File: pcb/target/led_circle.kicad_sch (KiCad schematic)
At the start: 20 parts

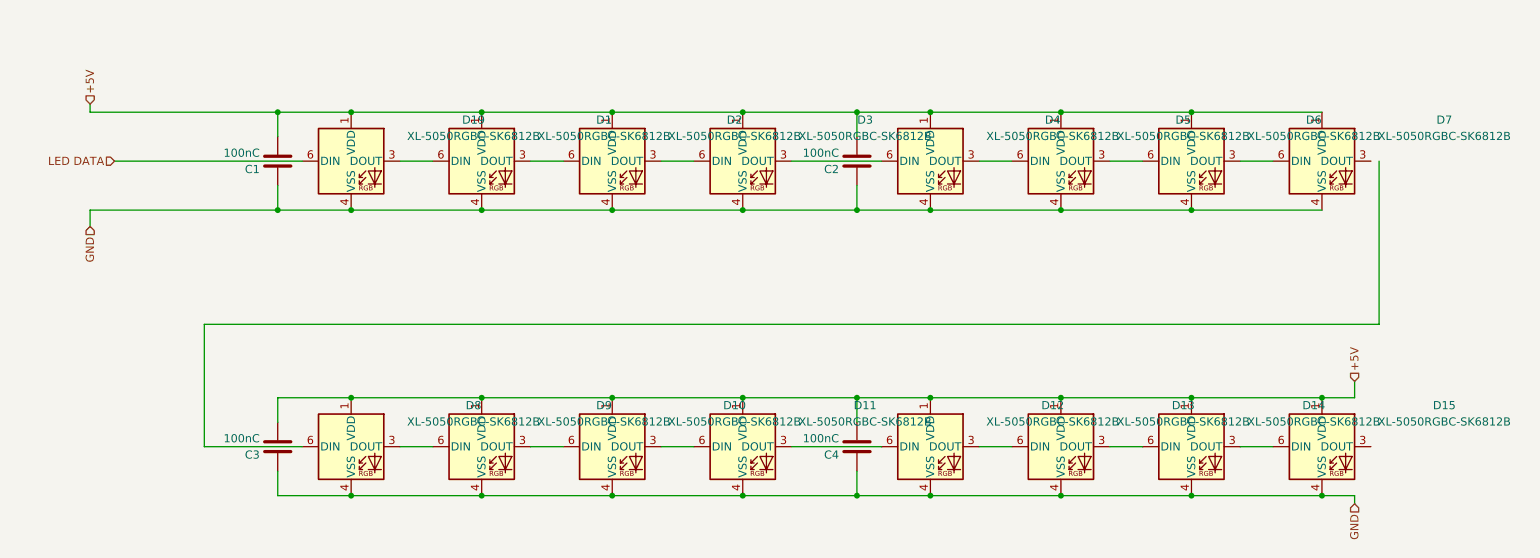
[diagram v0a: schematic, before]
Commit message: added updi connector
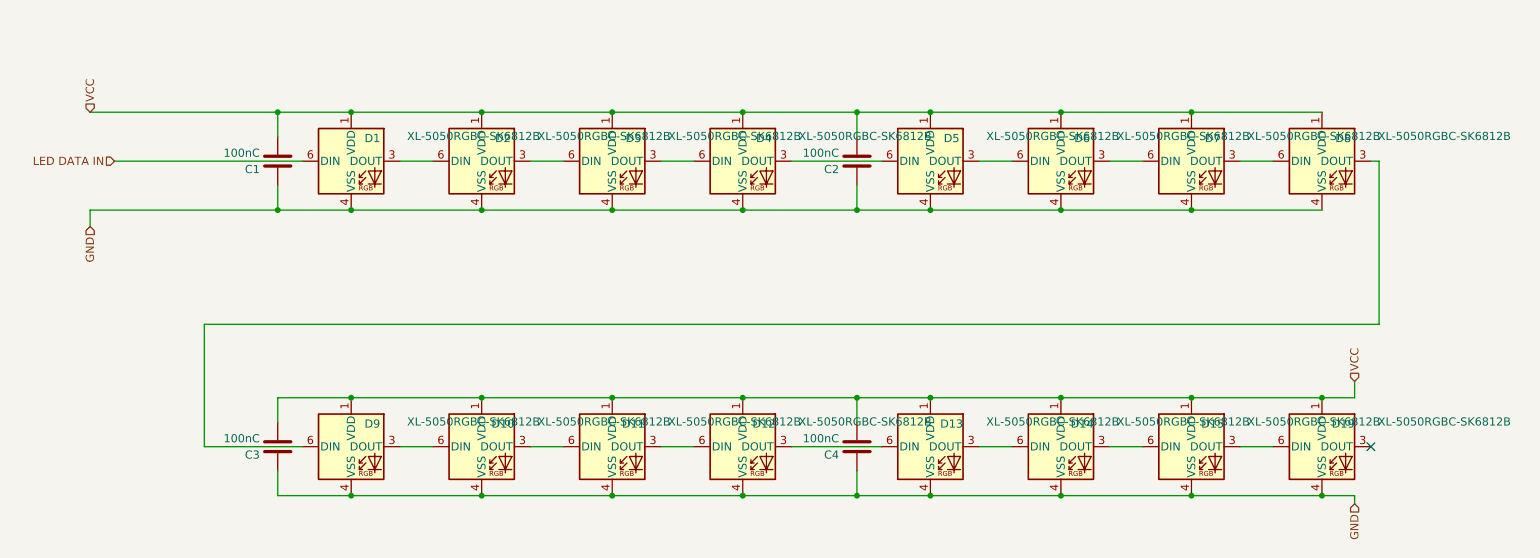
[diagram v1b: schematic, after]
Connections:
- net LED DATA is gone; now on an unnamed net: D19.6 (DIN)
- net at D7.3 (DOUT): now also D8.6 (DIN)
- net at D19.3 (DOUT): no longer D1.6 (DIN)
- net +5V renamed VCC
- new net LED DATA IN: D1.6 (DIN)
- no-connect marks 0 -> 1

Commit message: fixed some footprint issues
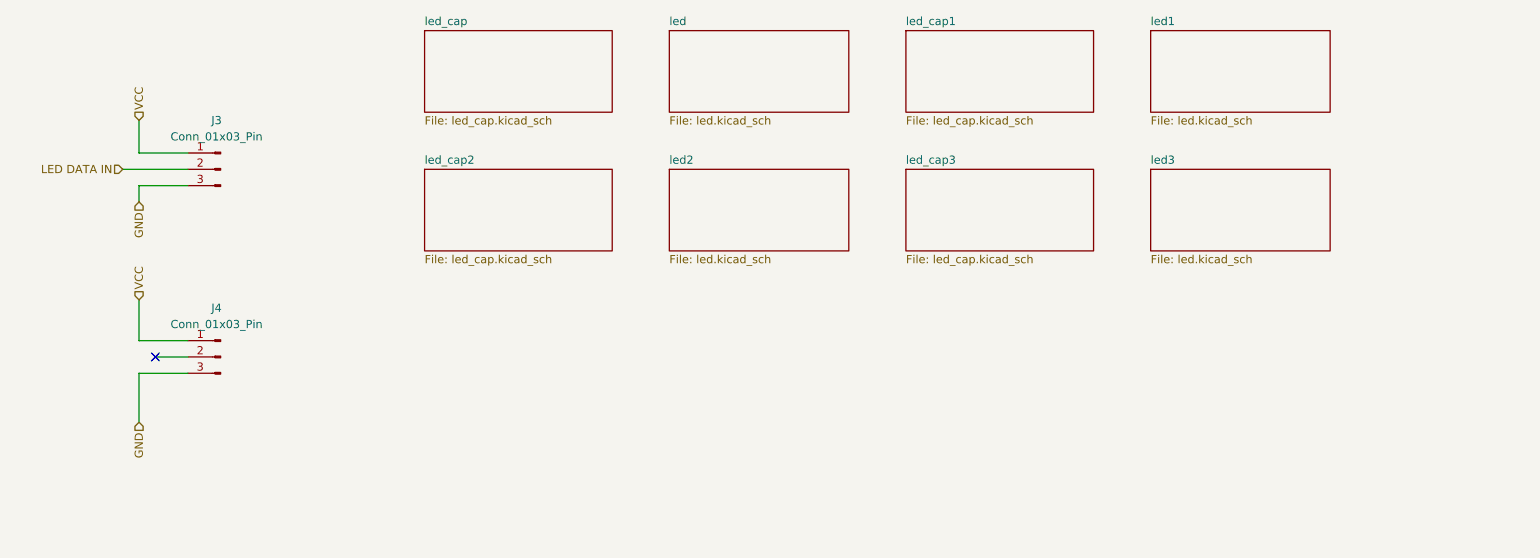
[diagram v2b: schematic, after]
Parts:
- removed C1, C2, C3, C4: 100nC, Capacitor_SMD:C_1206_3216Metric, symbol Device:C
- removed D1, D10, D11, D12, D13, D14, D15, D19, D2, D3, D4, D5, D6, D7, D8, D9: XL-5050RGBC-SK6812B, custom_footprints:XL-5050RGBC-SK6812B, symbol custom_symbols:XL-5050RGBC-SK6812B
- added J3, J4: Conn_01x03_Pin, Connector_Wire:SolderWire-0.75sqmm_1x03_P4.8mm_D1.25mm_OD2.3mm, symbol Connector:Conn_01x03_Pin
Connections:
- net GND: now also J3.3 (Pin_3), J4.3 (Pin_3)
- net LED DATA IN: now also J3.2 (Pin_2)
- net VCC: now also J3.1 (Pin_1), J4.1 (Pin_1)
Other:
- added sheet led (led.kicad_sch)
- added sheet led1 (led.kicad_sch)
- added sheet led2 (led.kicad_sch)
- added sheet led3 (led.kicad_sch)
- added sheet led_cap (led_cap.kicad_sch)
- added sheet led_cap1 (led_cap.kicad_sch)
- added sheet led_cap2 (led_cap.kicad_sch)
- added sheet led_cap3 (led_cap.kicad_sch)

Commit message: finishing up target pcb
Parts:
- J3, J4: footprint Connector_Wire:SolderWire-0.75sqmm_1x03_P4.8mm_D1.25mm_OD2.3mm -> custom_footprints:01x03 SMD 2x3mm pad
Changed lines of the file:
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@@
 			)
 		)
-		(property "Footprint" "Connector_Wire:SolderWire-0.75sqmm_1x03_P4.8mm_D1.25mm_OD2.3mm"
+		(property "Footprint" "custom_footprints:01x03 SMD 2x3mm pad"
 			(at 43.18 74.93 0)
 			(effects
@@
 			)
 		)
-		(property "Footprint" "Connector_Wire:SolderWire-0.75sqmm_1x03_P4.8mm_D1.25mm_OD2.3mm"
+		(property "Footprint" "custom_footprints:01x03 SMD 2x3mm pad"
 			(at 43.18 45.72 0)
 			(effects

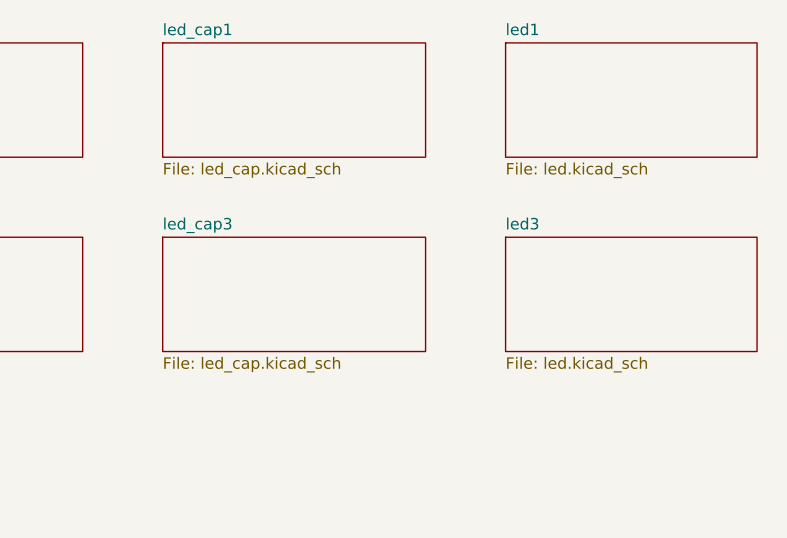
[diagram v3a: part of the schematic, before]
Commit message: added lcsc numbers to all components and added ESD protection
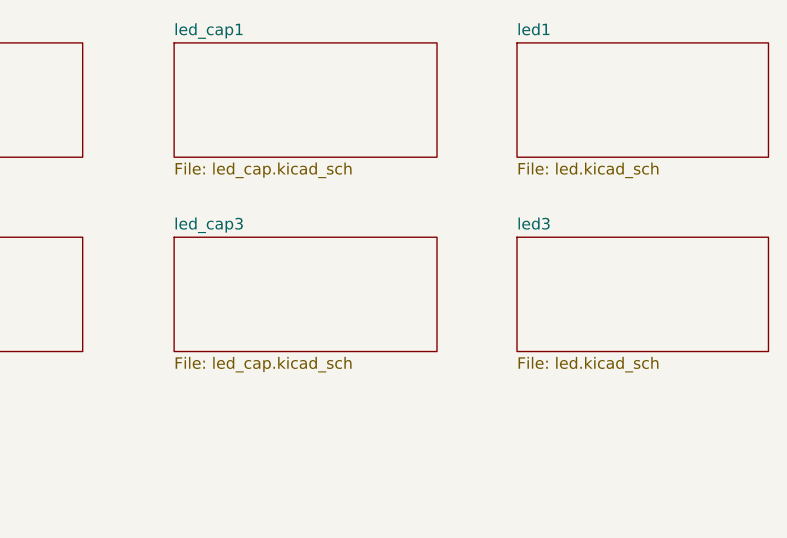
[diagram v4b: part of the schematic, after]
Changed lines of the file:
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@@
+			)
+		)
+		(property "LCSC" ""
+			(at 43.18 74.93 0)
+			(effects
+				(font
+					(size 1.27 1.27)
+				)
+				(hide yes)
 			)
 		)
@@
 			)
 		)
+		(property "LCSC" ""
+			(at 43.18 45.72 0)
+			(effects
+				(font
+					(size 1.27 1.27)
+				)
+				(hide yes)
+			)
+		)
 		(pin "3"
 		)
@@
 	)
 	(sheet
-		(at 149.86 24.13)
+		(at 151.13 24.13)
 		(size 29.21 12.7)
 		(exclude_from_sim no)
@@
 		)
 		(property "Sheetname" "led_cap1"
-			(at 149.86 23.4184 0)
+			(at 151.13 23.4184 0)
 			(effects
 				(font
@@
 		)
 		(property "Sheetfile" "led_cap.kicad_sch"
-			(at 149.86 37.4146 0)
+			(at 151.13 37.4146 0)
 			(effects
 				(font
@@
 	)
 	(sheet
-		(at 187.96 24.13)
+		(at 189.23 45.72)
 		(size 27.94 12.7)
 		(exclude_from_sim no)
@@
 			(color 0 0 0 0.0000)
 		)
-		(property "Sheetname" "led1"
-			(at 187.96 23.4184 0)
+		(property "Sheetname" "led3"
+			(at 189.23 45.0084 0)
 			(effects
 				(font
@@
 		)
 		(property "Sheetfile" "led.kicad_sch"
-			(at 187.96 37.4146 0)
-			(effects
-				(font
-					(size 1.27 1.27)
-				)
-				(justify left top)
-			)
-		)
-		(instances
-			(project "target"
-				(path "/1c02f793-f381-44cb-838a-dbb787484d0c/e61b723f-f359-4114-beb0-b4d2930b2aa9"
-					(page "6")
-				)
-			)
-		)
-	)
-	(sheet
-		(at 187.96 45.72)
-		(size 27.94 12.7)
-		(exclude_from_sim no)
-		(in_bom yes)
-		(on_board yes)
-		(dnp no)
-		(fields_autoplaced yes)
-		(stroke
-			(width 0.1524)
-			(type solid)
-		)
-		(fill
-			(color 0 0 0 0.0000)
-		)
-		(property "Sheetname" "led3"
-			(at 187.96 45.0084 0)
-			(effects
-				(font
-					(size 1.27 1.27)
-				)
-				(justify left bottom)
-			)
-		)
-		(property "Sheetfile" "led.kicad_sch"
-			(at 187.96 59.0046 0)
-			(effects
-				(font
-					(size 1.27 1.27)
-				)
-				(justify left top)
-			)
-		)
-		(instances
-			(project "target"
-				(path "/1c02f793-f381-44cb-838a-dbb787484d0c/e61b723f-f359-4114-beb0-b4d2930b2aa9"
-					(page "9")
-				)
-			)
-		)
-	)
-	(sheet
-		(at 149.86 45.72)
-		(size 29.21 12.7)
-		(exclude_from_sim no)
-		(in_bom yes)
-		(on_board yes)
-		(dnp no)
-		(fields_autoplaced yes)
-		(stroke
-			(width 0.1524)
-			(type solid)
-		)
-		(fill
-			(color 0 0 0 0.0000)
-		)
-		(property "Sheetname" "led_cap3"
-			(at 149.86 45.0084 0)
-			(effects
-				(font
-					(size 1.27 1.27)
-				)
-				(justify left bottom)
-			)
-		)
-		(property "Sheetfile" "led_cap.kicad_sch"
-			(at 149.86 59.0046 0)
-			(effects
-				(font
-					(size 1.27 1.27)
-				)
-				(justify left top)
-			)
-		)
-		(instances
-			(project "target"
-				(path "/1c02f793-f381-44cb-838a-dbb787484d0c/e61b723f-f359-4114-beb0-b4d2930b2aa9"
-					(page "11")
+			(at 189.23 59.0046 0)
+			(effects
+				(font
+					(size 1.27 1.27)
+				)
+				(justify left top)
+			)
+		)
+		(instances
+			(project "target"
+				(path "/1c02f793-f381-44cb-838a-dbb787484d0c/e61b723f-f359-4114-beb0-b4d2930b2aa9"
+					(page "10")
 				)
 			)
@@
 			(project "target"
 				(path "/1c02f793-f381-44cb-838a-dbb787484d0c/e61b723f-f359-4114-beb0-b4d2930b2aa9"
-					(page "10")
+					(page "9")
+				)
+			)
+		)
+	)
+	(sheet
+		(at 189.23 24.13)
+		(size 27.94 12.7)
+		(exclude_from_sim no)
+		(in_bom yes)
+		(on_board yes)
+		(dnp no)
+		(fields_autoplaced yes)
+		(stroke
+			(width 0.1524)
+			(type solid)
+		)
+		(fill
+			(color 0 0 0 0.0000)
+		)
+		(property "Sheetname" "led1"
+			(at 189.23 23.4184 0)
+			(effects
+				(font
+					(size 1.27 1.27)
+				)
+				(justify left bottom)
+			)
+		)
+		(property "Sheetfile" "led.kicad_sch"
+			(at 189.23 37.4146 0)
+			(effects
+				(font
+					(size 1.27 1.27)
+				)
+				(justify left top)
+			)
+		)
+		(instances
+			(project "target"
+				(path "/1c02f793-f381-44cb-838a-dbb787484d0c/e61b723f-f359-4114-beb0-b4d2930b2aa9"
+					(page "6")
+				)
+			)
+		)
+	)
+	(sheet
+		(at 151.13 45.72)
+		(size 29.21 12.7)
+		(exclude_from_sim no)
+		(in_bom yes)
+		(on_board yes)
+		(dnp no)
+		(fields_autoplaced yes)
+		(stroke
+			(width 0.1524)
+			(type solid)
+		)
+		(fill
+			(color 0 0 0 0.0000)
+		)
+		(property "Sheetname" "led_cap3"
+			(at 151.13 45.0084 0)
+			(effects
+				(font
+					(size 1.27 1.27)
+				)
+				(justify left bottom)
+			)
+		)
+		(property "Sheetfile" "led_cap.kicad_sch"
+			(at 151.13 59.0046 0)
+			(effects
+				(font
+					(size 1.27 1.27)
+				)
+				(justify left top)
+			)
+		)
+		(instances
+			(project "target"
+				(path "/1c02f793-f381-44cb-838a-dbb787484d0c/e61b723f-f359-4114-beb0-b4d2930b2aa9"
+					(page "11")
+				)
+			)
+		)
+	)
+	(sheet
+		(at 74.93 24.13)
+		(size 29.21 12.7)
+		(exclude_from_sim no)
+		(in_bom yes)
+		(on_board yes)
+		(dnp no)
+		(fields_autoplaced yes)
+		(stroke
+			(width 0.1524)
+			(type solid)
+		)
+		(fill
+			(color 0 0 0 0.0000)
+		)
+		(property "Sheetname" "led_cap"
+			(at 74.93 23.4184 0)
+			(effects
+				(font
+					(size 1.27 1.27)
+				)
+				(justify left bottom)
+			)
+		)
+		(property "Sheetfile" "led_cap.kicad_sch"
+			(at 74.93 37.4146 0)
+			(effects
+				(font
+					(size 1.27 1.27)
+				)
+				(justify left top)
+			)
+		)
+		(instances
+			(project "target"
+				(path "/1c02f793-f381-44cb-838a-dbb787484d0c/e61b723f-f359-4114-beb0-b4d2930b2aa9"
+					(page "4")
+				)
+			)
+		)
+	)
+	(sheet
+		(at 113.03 24.13)
+		(size 27.94 12.7)
+		(exclude_from_sim no)
+		(in_bom yes)
+		(on_board yes)
+		(dnp no)
+		(fields_autoplaced yes)
+		(stroke
+			(width 0.1524)
+			(type solid)
+		)
+		(fill
+			(color 0 0 0 0.0000)
+		)
+		(property "Sheetname" "led"
+			(at 113.03 23.4184 0)
+			(effects
+				(font
+					(size 1.27 1.27)
+				)
+				(justify left bottom)
+			)
+		)
+		(property "Sheetfile" "led.kicad_sch"
+			(at 113.03 37.4146 0)
+			(effects
+				(font
+					(size 1.27 1.27)
+				)
+				(justify left top)
+			)
+		)
+		(instances
+			(project "target"
+				(path "/1c02f793-f381-44cb-838a-dbb787484d0c/e61b723f-f359-4114-beb0-b4d2930b2aa9"
+					(page "5")
 				)
 			)
@@
 				)
 			)
-		)
-	)
-	(sheet
-		(at 74.93 24.13)
-		(size 29.21 12.7)
-		(exclude_from_sim no)
-		(in_bom yes)
-		(on_board yes)
-		(dnp no)
-		(fields_autoplaced yes)
-		(stroke
-			(width 0.1524)
-			(type solid)
-		)
-		(fill
-			(color 0 0 0 0.0000)
-		)
-		(property "Sheetname" "led_cap"
-			(at 74.93 23.4184 0)
-			(effects
-				(font
-					(size 1.27 1.27)
-				)
-				(justify left bottom)
-			)
-		)
-		(property "Sheetfile" "led_cap.kicad_sch"
-			(at 74.93 37.4146 0)
-			(effects
-				(font
-					(size 1.27 1.27)
-				)
-				(justify left top)
-			)
-		)
-		(instances
-			(project "target"
-				(path "/1c02f793-f381-44cb-838a-dbb787484d0c/e61b723f-f359-4114-beb0-b4d2930b2aa9"
-					(page "4")
-				)
-			)
-		)
-	)
-	(sheet
-		(at 113.03 24.13)
-		(size 27.94 12.7)
-		(exclude_from_sim no)
-		(in_bom yes)
-		(on_board yes)
-		(dnp no)
-		(fields_autoplaced yes)
-		(stroke
-			(width 0.1524)
-			(type solid)
-		)
-		(fill
-			(color 0 0 0 0.0000)
-		)
-		(property "Sheetname" "led"
-			(at 113.03 23.4184 0)
-			(effects
-				(font
-					(size 1.27 1.27)
-				)
-				(justify left bottom)
-			)
-		)
-		(property "Sheetfile" "led.kicad_sch"
-			(at 113.03 37.4146 0)
-			(effects
-				(font
-					(size 1.27 1.27)
-				)
-				(justify left top)
-			)
-		)
-		(instances
-			(project "target"
-				(path "/1c02f793-f381-44cb-838a-dbb787484d0c/e61b723f-f359-4114-beb0-b4d2930b2aa9"
-					(page "5")
-				)
-			)

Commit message: finished all pcbs by adjusting traces acording to 1oz copper weight
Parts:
- J3, J4: now left out of the parts list
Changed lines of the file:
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@@
 		(unit 1)
 		(exclude_from_sim no)
-		(in_bom yes)
+		(in_bom no)
 		(on_board yes)
 		(dnp no)
@@
 		(unit 1)
 		(exclude_from_sim no)
-		(in_bom yes)
+		(in_bom no)
 		(on_board yes)
 		(dnp no)
